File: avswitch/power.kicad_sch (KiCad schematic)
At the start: 57 parts, among them J401 694106301002, U401 TPS561243DRLR, U402 LM2611xMF

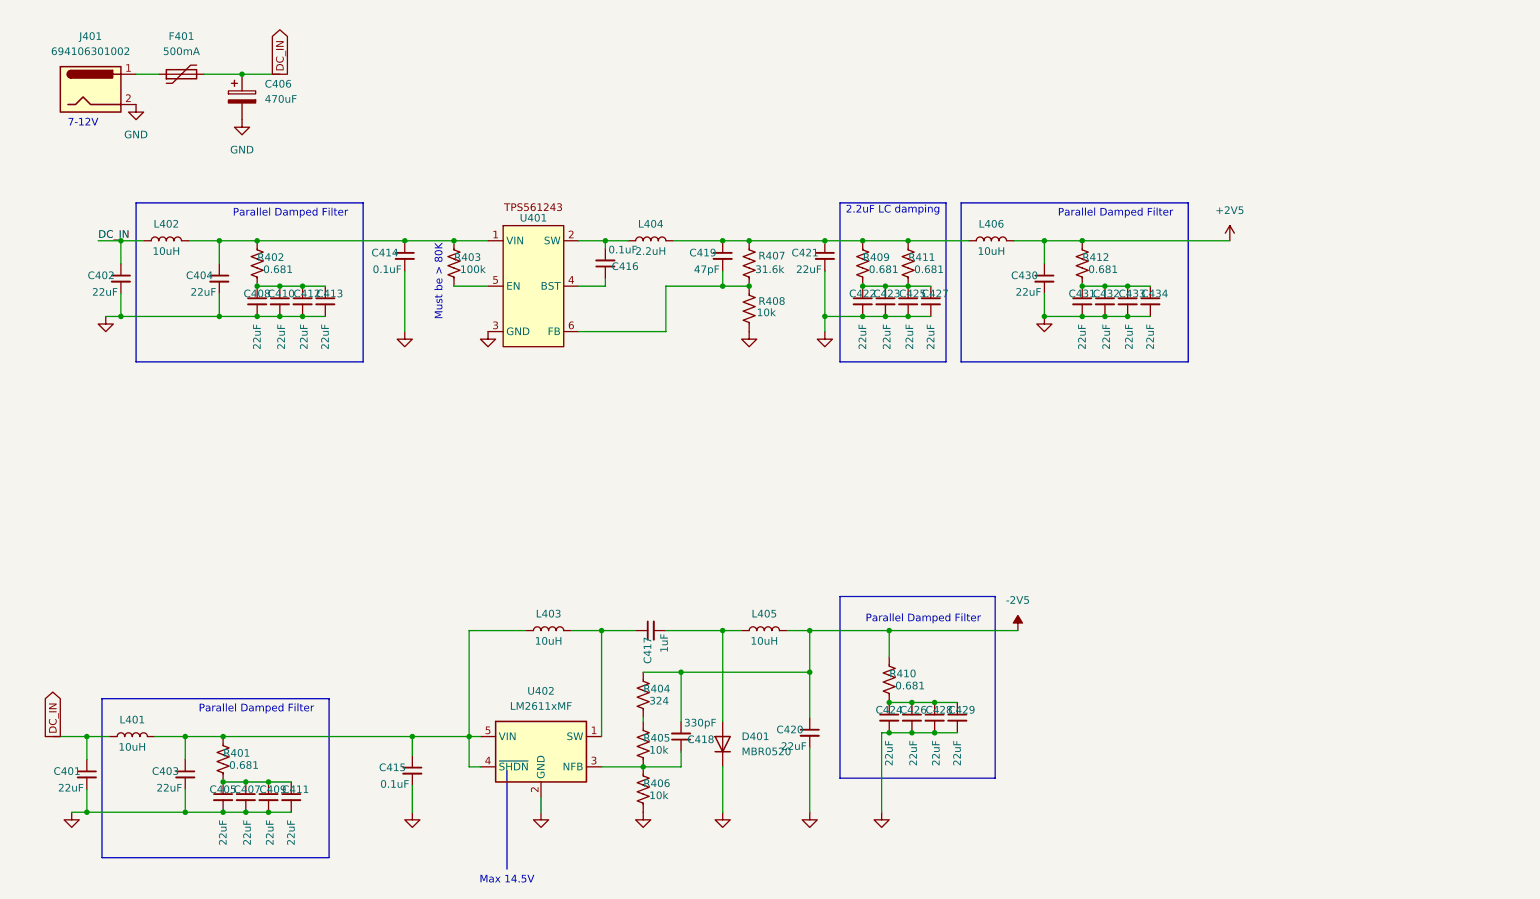
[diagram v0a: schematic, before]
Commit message: Recalculate for ceramic cap dc bias
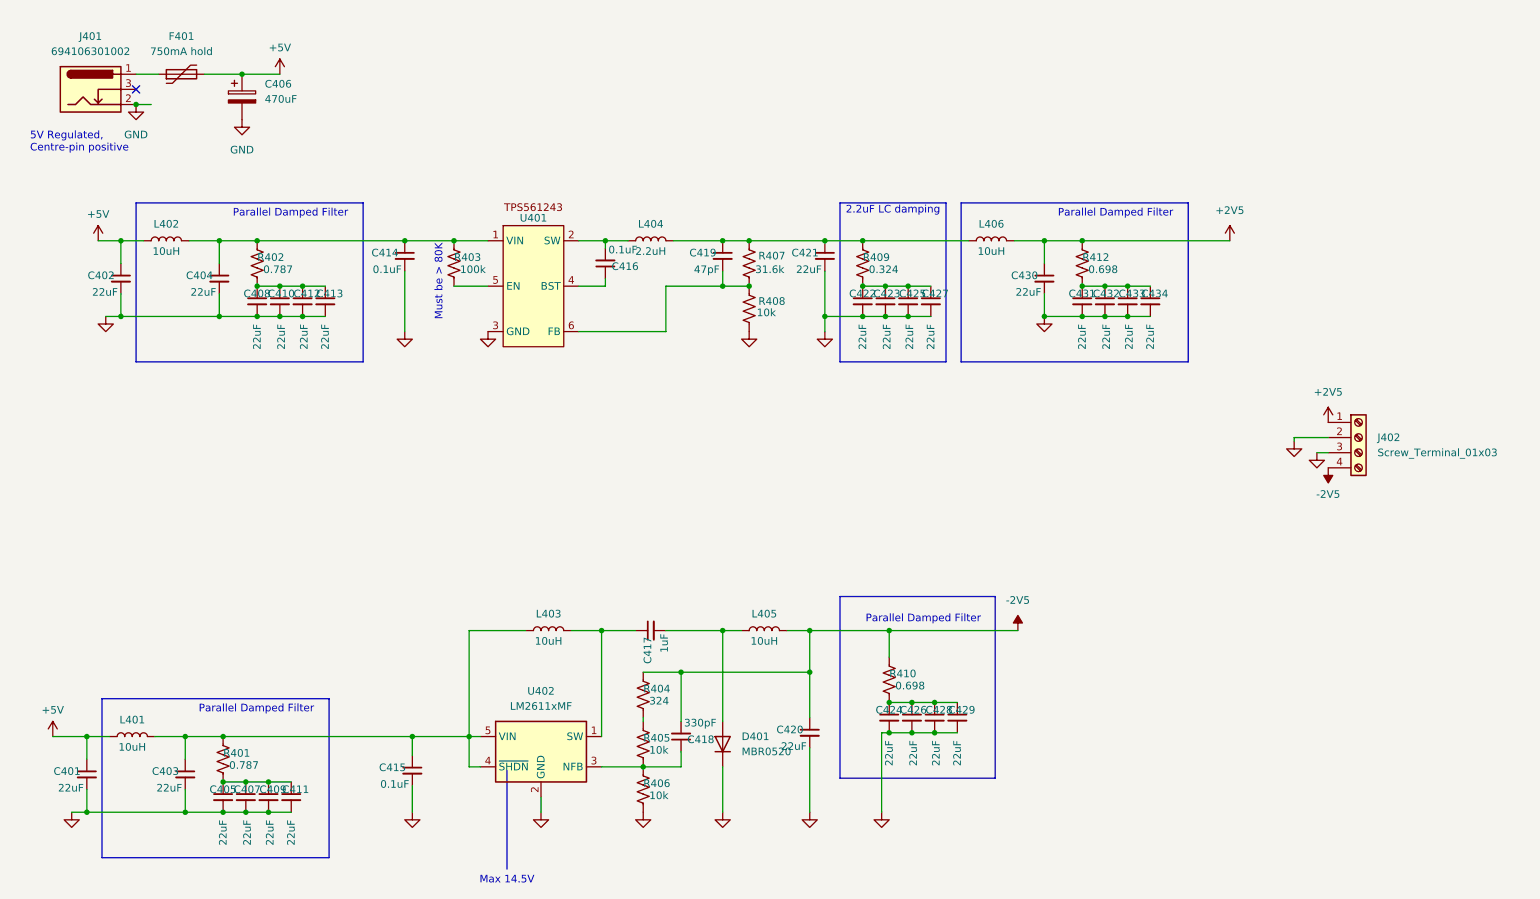
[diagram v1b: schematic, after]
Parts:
- removed R411: 0.681, Resistor_SMD:R_0805_2012Metric, symbol Device:R_US
- added J402: Screw_Terminal_01x03, TerminalBlock:TerminalBlock_MaiXu_MX126-5.0-04P_1x04_P5.00mm, symbol Connector:Screw_Terminal_01x04
- F401: value 500mA -> 750mA hold
- J401: symbol Connector:Barrel_Jack -> Connector:Barrel_Jack_Switch
- R401, R402: value 0.681 -> 0.787
- R409: value 0.681 -> 0.324
- R410, R412: value 0.681 -> 0.698
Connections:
- net +2V5: now also J402.1 (Pin_1)
- net -2V5: now also J402.4 (Pin_4)
- net GND: now also J402.2 (Pin_2), J402.3 (Pin_3)
- net DC_IN renamed +5V
- no-connect marks 0 -> 1
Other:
- note added: "5V Regulated, Centre-pin positive"
- note removed: "7-12V"

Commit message: PCB Layout nearing completion
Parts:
- removed C422, C423, C425, C427: 22uF, Capacitor_SMD:C_1210_3225Metric, symbol Device:C_Small
- removed J401: 694106301002, Connector_BarrelJack:BarrelJack_Wuerth_6941xx301002, symbol Connector:Barrel_Jack_Switch
- removed R409: 0.324, Resistor_SMD:R_0805_2012Metric, symbol Device:R_US
- added C435: 0.1uF, Capacitor_SMD:C_0402_1005Metric, symbol Device:C_Small
- added C436: 10uF, Capacitor_SMD:C_1210_3225Metric, symbol Device:C_Small
- added J403: SamySky UJC-H-G-SMT-2-P6-TR, Connector_USB:USB_C_Receptacle_GCT_USB4125-xx-x_6P_TopMnt_Horizontal, symbol Connector:USB_C_Receptacle_PowerOnly_6P
- added R411, R413: 5.1k, Resistor_SMD:R_0805_2012Metric, symbol Device:R_US
- added R416: 10k, Resistor_SMD:R_0805_2012Metric, symbol Device:R_US
- added U403: SRV05-4, Package_TO_SOT_SMD:SOT-23-6, symbol Power_Protection:SRV05-4
- added U404: AP22816BKEWT, Package_TO_SOT_SMD:SOT-23-5, symbol Power_Management:AP22816BKEWT
- C406: value 470uF -> 100uF; footprint Capacitor_THT:CP_Radial_D8.0mm_P3.50mm -> Capacitor_THT:CP_Radial_D6.3mm_P2.50mm
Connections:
- net +2V5: now also J402.4 (Pin_4); no longer J402.1 (Pin_1)
- net +5V: now also C435.2, U404.1 (OUT); no longer F401.2
- net -2V5: now also J402.1 (Pin_1); no longer J402.4 (Pin_4)
- net GND: now also C435.1, C436.2, J403.A12 (GND), J403.B12 (GND), J403.S1 (SHIELD), R411.2, R413.2, U403.2 (VN), U404.2 (GND), U404.4 (~{EN})
- net at F401.1: now also J403.A9 (VBUS), J403.B9 (VBUS)
- new net: R416.1, U404.3 (~{FLG})
- new net CC1: J403.A5 (CC1), R411.1, U403.1 (IO1)
- new net CC2: J403.B5 (CC2), R413.1, U403.3 (IO2)
- new net VBUS: C436.1, F401.2, R416.2, U403.5 (VP), U404.5 (IN)
- no-connect marks 1 -> 2
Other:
- note added: ""A" version is EN active high "B" version is EN active Low 816 = 1A 817 = 1.5A 818 - 2A"
- note added: "10uF VBus Limit"
- note added: "ESD Protection"
- note added: "Inrush current limiting"
- note removed: "2.2uF LC damping"
- note removed: "5V Regulated, Centre-pin positive"
- moved on the sheet: C402, C404, C406, C408, C410, C412, C413, C414, C416, C419, C421, C430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

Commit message: V0.1 ordered from jlpcb
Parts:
- C417: value 1uF -> 1.0uF
- J403: value SamySky UJC-H-G-SMT-2-P6-TR -> SameSky UJC-H-G-SMT-2-P6-TR
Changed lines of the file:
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@@
 			)
 		)
-		(property "Value" "SamySky UJC-H-G-SMT-2-P6-TR"
+		(property "Value" "SameSky UJC-H-G-SMT-2-P6-TR"
 			(at 28.575 18.415 0)
 			(effects
@@
 			)
 		)
-		(property "Value" "1uF"
+		(property "Value" "1.0uF"
 			(at 119.126 116.713 0)
 			(effects

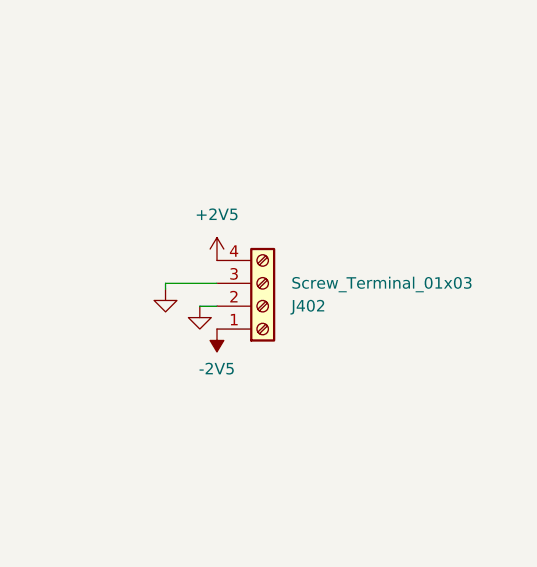
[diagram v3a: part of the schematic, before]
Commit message: v2 pcb - fix up RCA footprint, screw terminal bom
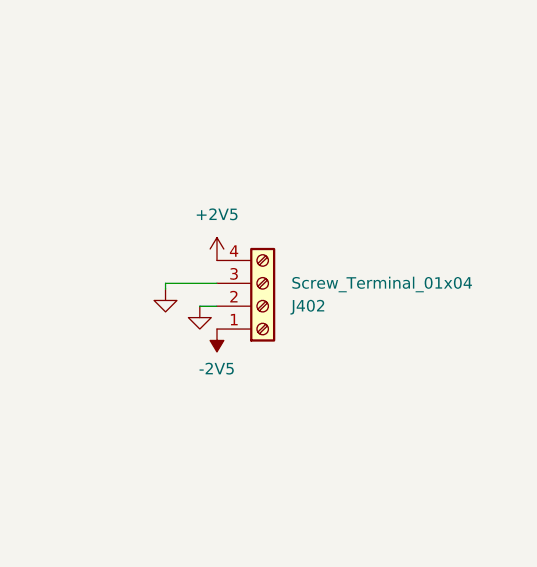
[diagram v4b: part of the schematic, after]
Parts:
- J402: value Screw_Terminal_01x03 -> Screw_Terminal_01x04
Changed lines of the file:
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@@
 			)
 		)
-		(property "Value" "Screw_Terminal_01x03"
+		(property "Value" "Screw_Terminal_01x04"
 			(at 238.76 83.8201 0)
 			(effects
